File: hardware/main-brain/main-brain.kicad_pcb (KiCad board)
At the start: 2 copper layers, 140 x 70 mm, 31 parts, among them J1 19V, J2 CAN+5V, J3 19V OUT, J4 I2S OUT, Q1 SI2301 class, Q2 2N7000, U1 SN65HVD230

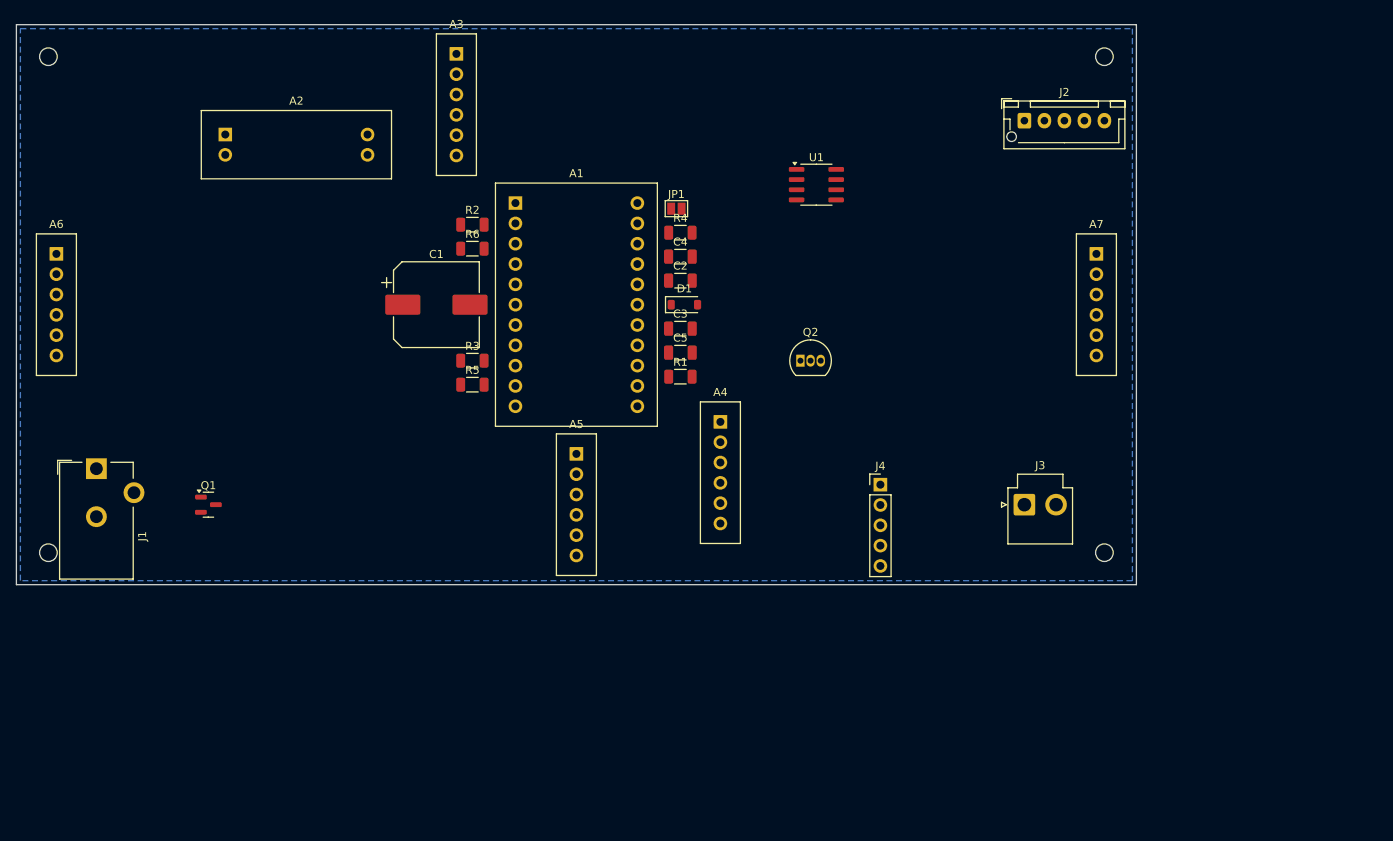
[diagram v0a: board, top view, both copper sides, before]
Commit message: Rebuild both boards from the real driver module, grouped by function
The vendor's EasyEDA export of the driver module arrived, so its footprint is
now measured rather than guessed: 17 pins and four mounting holes over
22.6 x 18.2 mm, read from vendor/simplefoc_stepmini.json at build time.

The export also settles three things that were open, and raises one:

- The module's 3V3 pin is a supply input. Its nSLEEP and nRESET pull-ups hang
  off it and there is no regulator on the board, so leaving it open would have
  left the driver possibly held in reset. It is now wired to the 3.3 V rail.
- The header's enable pin sits behind a series resistor into the driver's EN,
  so the kill line drives it directly and nSLEEP/nRESET need no connection.
- nFAULT is brought out with its own pull-up, so it now goes to PB4.
- The export shows a quad half-bridge - IN1-IN4 and OUT1-OUT4 - not the
  three-in/three-out DRV8313 the build console names. A 3-phase motor uses
  three of the four channels, so it works, but it is not the specified part.
  Flagged in the actuator README rather than silently accepted.

Placement is now by functional block. Each block keeps its own passives, and
parts with an electrical reason to hug another are placed against it and
checked: the crystal is held within 12 mm of the MCU and its load caps within
9 mm of it, which the previous layout failed at 32 mm. Microphone spacing is
pinned at exactly 130 mm and verified. Both boards are larger - the node goes
to 70 x 60 and the base to 170 x 100 - which is what buys room to group and
still route by hand.

Indicators added on both boards, using the XL-3216SURC red 1206 that is on
hand. Series resistors are sized for its 2.4 V forward drop rather than left at
a default: 220 R on 3.3 V rails, 470 R on the 5 V one.

check.py grew to match: it now verifies group membership, pinned positions and
proximity constraints alongside the netlist, and each project carries a
colour-coded placement.svg.

Co-Authored-By: Claud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
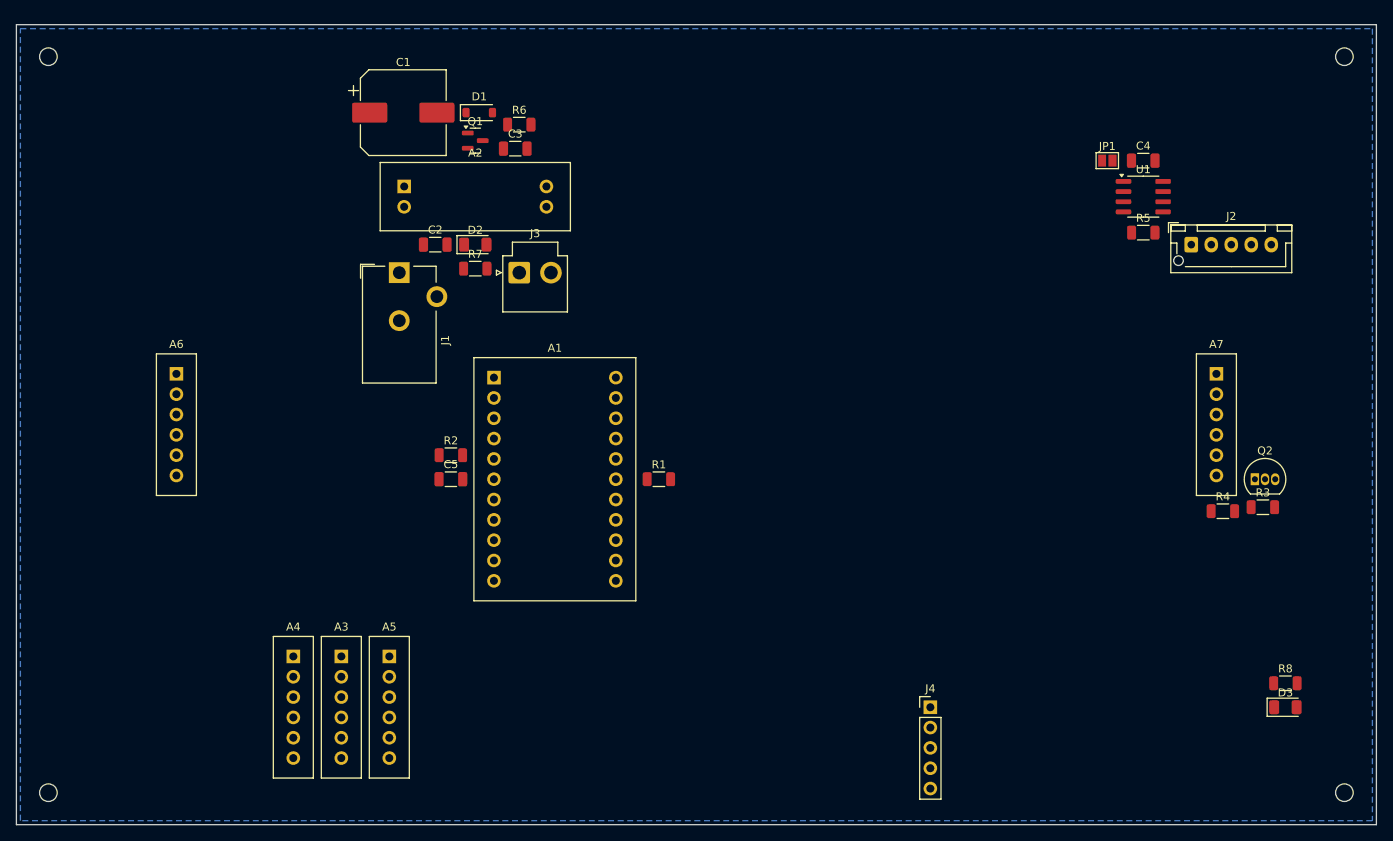
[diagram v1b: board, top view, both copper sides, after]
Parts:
- added D2: XL-3216SURC red, LED_SMD:LED_1206_3216Metric, F.Cu at (57.4, 27.5)
- added D3: XL-3216SURC red, LED_SMD:LED_1206_3216Metric, F.Cu at (158.6, 85.3)
- added R7: 470R, Resistor_SMD:R_1206_3216Metric, F.Cu at (57.4, 30.5)
- added R8: 220R, Resistor_SMD:R_1206_3216Metric, F.Cu at (158.6, 82.3)
- moved R3 100.5 mm to (155.8, 60.3)
- moved R5 86.0 mm to (140.9, 26.0)
- moved A3 76.7 mm to (40.6, 85.3)
- moved R4 76.2 mm to (150.8, 60.8)
- moved J3 69.5 mm to (62.9, 31.0)
- moved A4 60.9 mm to (34.6, 85.3)
- moved C4 59.1 mm to (140.9, 17.0)
- moved Q2 58.7 mm to (154.8, 56.8)
- moved Q1 56.4 mm to (57.4, 14.5)
- moved JP1 54.2 mm to (136.4, 17.0)
- moved J1 45.1 mm to (47.9, 31.0)
- moved ? 42.4 mm to (166.0, 96.0)
- moved U1 40.9 mm to (140.9, 21.5)
- moved D1 35.1 mm to (57.9, 11.0)
- moved A5 34.5 mm to (46.6, 85.3)
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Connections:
- A1 pad 4: (no net) -> RUN_LED_A
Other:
- board size 140 x 70 mm -> 170 x 100 mm
- board text added: "audio"
- board text added: "can"
- board text added: "i2c"
- board text added: "kill"
- board text added: "mcu"
- board text added: "power"
- board text added: "status"

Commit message: Rebuild the driver module around the real SimpleFOC Mini v1.0
The EasyEDA export the footprint was generated from was a different product:
a "step mini" quad half-bridge with IN1-IN4 and four outputs, where the board
on the bench is a SimpleFOC Mini v1.0 (DRV8313, three phases, dated 04/22).
The generated footprint carried phantom IN4/OUT4 pins, the wrong row order and
the wrong geometry, and would not have populated.

Everything now comes from the v1.0 exports. The PCB export gives pad geometry;
the schematic export resolves that PCB's anonymous U1_nn nets to real signals
and is what settled the important question below. Both step-mini exports are
removed.

Fixes a real bug this uncovered. The module's 3V3 header pin is DRV8313 pin 15,
V3P3OUT - an internal regulator output, not a supply input as previously
assumed. It had been wired to the carrier's 3.3 V rail, which would have
connected the AMS1117's output to the module's own regulator. It is now left
open, and check.py fails the build if it reappears on any net. That same
regulator feeds the module's nSlp/nRes/nFlt pull-ups, which is why those three
need no connection to idle in the running state.

The module's reference becomes A1 rather than M1, so its pins can carry the
silkscreen names M1/M2/M3 without ("M1", "M1") appearing in the netlist.

Two generator fixes fell out of the rebuild:

- simplefoc_from_json() now reads pads nested inside LIB entries, because on
  this board the headers are placed as components - only 6 of the 19 pads are
  top-level shapes - while filtering to the HDR-* components so the driver IC's
  own 29 pads stay out.
- Proximity placement follows each chain depth-first and ranks candidates by
  distance to the target's courtyard rather than to its origin. Breadth-first
  ranking by origin put a crystal load cap 3.8 mm clear of a crystal whose
  courtyard is 20 mm wide; both caps now sit inside 2 mm. check.py measures the
  same way, edge to edge, since centre-to-centre was mostly mea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
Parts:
- moved R1 27.9 mm to (54.3, 46.8)
- moved C5 13.0 mm to (54.3, 43.8)
- moved JP1 5.50 mm to (141.9, 17.0)
- moved R2 4.00 mm to (54.3, 49.8)
- moved C4 3.50 mm to (137.4, 17.0)
- moved J2 3.50 mm to (143.4, 27.5)
- moved R5 3.50 mm to (137.4, 26.0)
- moved J1 3.00 mm to (44.9, 31.0)
- moved R6 2.12 mm to (61.4, 11.0)
- moved R7 2.00 mm to (55.4, 30.5)
- moved R8 2.00 mm to (156.6, 82.3)
- moved C1 1.50 mm to (46.9, 11.0)
- moved D1 1.50 mm to (56.4, 11.0)
- moved C2 1.00 mm to (51.4, 27.5)
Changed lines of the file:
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@@
 	(footprint "Capacitor_SMD:CP_Elec_10x10.5"
 		(layer "F.Cu")
-		(at 48.36 10.996)
+		(at 46.86 10.996)
 		(descr "SMD capacitor, aluminum electrolytic, Vishay 1010, 10.0x10.5mm, http://www.vishay.com/docs/28395/150crz.pdf")
 		(tags "capacitor electrolytic")
@@
 	(footprint "Capacitor_SMD:C_1206_3216Metric"
 		(layer "F.Cu")
-		(at 52.36 27.496)
+		(at 51.36 27.496)
 		(descr "Capacitor SMD 1206 (3216 Metric), square (rectangular) end terminal, IPC_7351 nominal, (Body size source: IPC-SM-782 page 76, https://www.pcb-3d.com/wordpress/wp-content/uploads/ipc-sm-782a_amendment_1_and_2.pdf), generated with kicad-footprint-generator")
 		(tags "capacitor")
@@
 	(footprint "Capacitor_SMD:C_1206_3216Metric"
 		(layer "F.Cu")
-		(at 140.86 16.996)
+		(at 137.36 16.996)
 		(descr "Capacitor SMD 1206 (3216 Metric), square (rectangular) end terminal, IPC_7351 nominal, (Body size source: IPC-SM-782 page 76, https://www.pcb-3d.com/wordpress/wp-content/uploads/ipc-sm-782a_amendment_1_and_2.pdf), generated with kicad-footprint-generator")
 		(tags "capacitor")
@@
 	(footprint "Capacitor_SMD:C_1206_3216Metric"
 		(layer "F.Cu")
-		(at 54.31 56.818)
+		(at 54.31 43.818)
 		(descr "Capacitor SMD 1206 (3216 Metric), square (rectangular) end terminal, IPC_7351 nominal, (Body size source: IPC-SM-782 page 76, https://www.pcb-3d.com/wordpress/wp-content/uploads/ipc-sm-782a_amendment_1_and_2.pdf), generated with kicad-footprint-generator")
 		(tags "capacitor")
@@
 	(footprint "Diode_SMD:D_SOD-123"
 		(layer "F.Cu")
-		(at 57.86 10.996)
+		(at 56.36 10.996)
 		(descr "SOD-123")
 		(tags "SOD-123")
@@
 	(footprint "Connector_BarrelJack:BarrelJack_CUI_PJ-102AH_Horizontal"
 		(layer "F.Cu")
-		(at 47.86 30.996)
+		(at 44.86 30.996)
 		(descr "Thin-pin DC Barrel Jack, https://cdn-shop.adafruit.com/datasheets/21mmdcjackDatasheet.pdf")
 		(tags "Power Jack")
@@
 	(footprint "Connector_JST:JST_XH_B5B-XH-AM_1x05_P2.50mm_Vertical"
 		(layer "F.Cu")
-		(at 146.86 27.496)
+		(at 143.36 27.496)
 		(descr "JST XH series connector, B5B-XH-AM, with boss (http://www.jst-mfg.com/product/pdf/eng/eXH.pdf), generated with kicad-footprint-generator")
 		(tags "connector JST XH vertical boss")
@@
 	(footprint "Jumper:SolderJumper-2_P1.3mm_Open_Pad1.0x1.5mm"
 		(layer "F.Cu")
-		(at 136.36 16.996)
+		(at 141.86 16.996)
 		(descr "SMD Solder Jumper, 1x1.5mm Pads, 0.3mm gap, open")
 		(tags "solder jumper open")
@@
 	(footprint "Resistor_SMD:R_1206_3216Metric"
 		(layer "F.Cu")
-		(at 80.31 56.818)
+		(at 54.31 46.818)
 		(descr "Resistor SMD 1206 (3216 Metric), square (rectangular) end terminal, IPC_7351 nominal, (Body size source: IPC-SM-782 page 72, https://www.pcb-3d.com/wordpress/wp-content/uploads/ipc-sm-782a_amendment_1_and_2.pdf), generated with kicad-footprint-generator")
 		(tags "resistor")
@@
 	(footprint "Resistor_SMD:R_1206_3216Metric"
 		(layer "F.Cu")
-		(at 54.31 53.818)
+		(at 54.31 49.818)
 		(descr "Resistor SMD 1206 (3216 Metric), square (rectangular) end terminal, IPC_7351 nominal, (Body size source: IPC-SM-782 page 72, https://www.pcb-3d.com/wordpress/wp-content/uploads/ipc-sm-782a_amendment_1_and_2.pdf), generated with kicad-footprint-generator")
 		(tags "resistor")
@@
 	(footprint "Resistor_SMD:R_1206_3216Metric"
 		(layer "F.Cu")
-		(at 140.86 25.996)
+		(at 137.36 25.996)
 		(descr "Resistor SMD 1206 (3216 Metric), square (rectangular) end terminal, IPC_7351 nominal, (Body size source: IPC-SM-782 page 72, https://www.pcb-3d.com/wordpress/wp-content/uploads/ipc-sm-782a_amendment_1_and_2.pdf), generated with kicad-footprint-generator")
 		(tags "resistor")
@@
 	(footprint "Resistor_SMD:R_1206_3216Metric"
 		(layer "F.Cu")
-		(at 62.86 12.496)
+		(at 61.36 10.996)
 		(descr "Resistor SMD 1206 (3216 Metric), square (rectangular) end terminal, IPC_7351 nominal, (Body size source: IPC-SM-782 page 72, https://www.pcb-3d.com/wordpress/wp-content/uploads/ipc-sm-782a_amendment_1_and_2.pdf), generated with kicad-footprint-generator")
 		(tags "resistor")
@@
 	(footprint "Resistor_SMD:R_1206_3216Metric"
 		(layer "F.Cu")
-		(at 57.36 30.496)
+		(at 55.36 30.496)
 		(descr "Resistor SMD 1206 (3216 Metric), square (rectangular) end terminal, IPC_7351 nominal, (Body size source: IPC-SM-782 page 72, https://www.pcb-3d.com/wordpress/wp-content/uploads/ipc-sm-782a_amendment_1_and_2.pdf), generated with kicad-footprint-generator")
 		(tags "resistor")
@@
 	(footprint "Resistor_SMD:R_1206_3216Metric"
 		(layer "F.Cu")
-		(at 158.628 82.322)
+		(at 156.628 82.322)
 		(descr "Resistor SMD 1206 (3216 Metric), square (rectangular) end terminal, IPC_7351 nominal, (Body size source: IPC-SM-782 page 72, https://www.pcb-3d.com/wordpress/wp-content/uploads/ipc-sm-782a_amendment_1_and_2.pdf), generated with kicad-footprint-generator")
 		(tags "resistor")

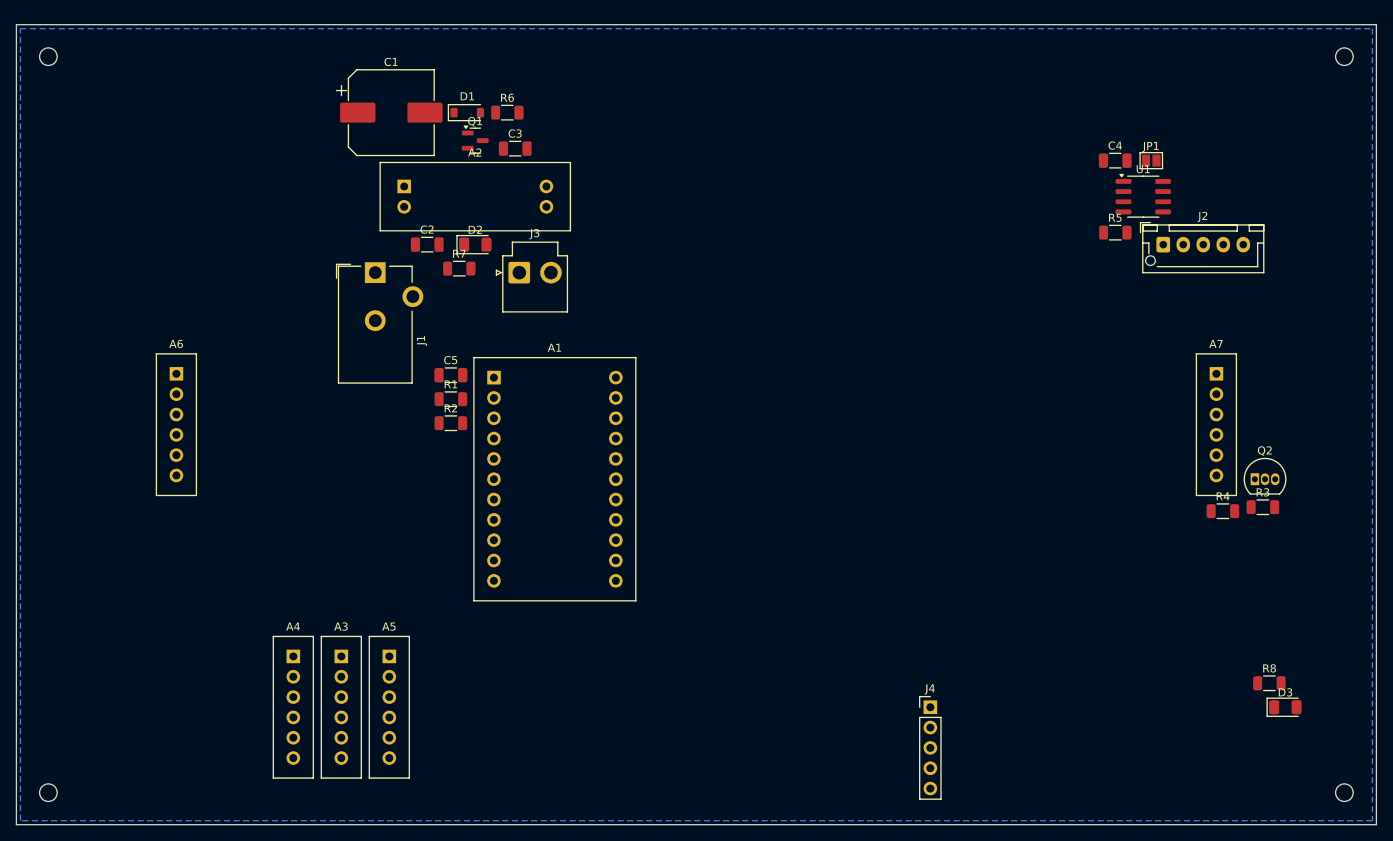
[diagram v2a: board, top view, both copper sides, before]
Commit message: Rebuild the BOM around parts on hand, and target Lion Circuits
Every passive and semiconductor in both boards is now a part that is actually
on the shelf, with docs/parts.md recording the reconciliation. Four
substitutions were needed:

- LED series resistors move from 220R/470R, which are not stocked, to 120R on
  the 3.3 V rails (7.5 mA) and 1k on the brain's 5 V rail (2.6 mA, where 120R
  would exceed the LED's 20 mA rating).
- The kill-line gate series resistor moves from 100R to 120R, immaterial here.
- The reverse-polarity FET becomes the AO3481 that is actually on hand; KiCad
  has no symbol for it, so the projects use AO3401A, the same family and the
  same G/S/D pinout.
- The 10 V zener clamping that FET's gate is not stocked, so the gate is
  divided rather than clamped: 100k source-to-gate and 100k gate-to-ground put
  Vgs at about -9.5 V, which enhances the FET hard and stays well inside its
  rating. Two resistors that are stocked, replacing one part that is not.

Two items have no substitute and must be ordered: 30 mR shunts, without which
there is no current sensing, and an N-channel MOSFET for the kill line, since
the AO3481 on hand is P-channel and cannot pull the EN bus down. The kill line
is the one circuit that should not be improvised.

Also notes that the CD43 inductor supplied with the transceivers has no place
in either board, and why the one plausible use - an LC filter on the node's
5 V input - would resonate at about 28 kHz, right on top of the motor PWM.

For fabrication, the boards now carry plot settings that emit Protel-style
gerber extensions, matching the sample set from Lion Circuits, with the X2
attributes off so the output is plain RS-274X. docs/fabrication.md records
their file naming and the design rules used, and is explicit that their
capability page could not be reached from here, so those rules are a
conservative set rather than a reading of their spec sheet.

Co-Authored-By: Claude Opus 5 <noreply@anthropic.com>
Claude-Sess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
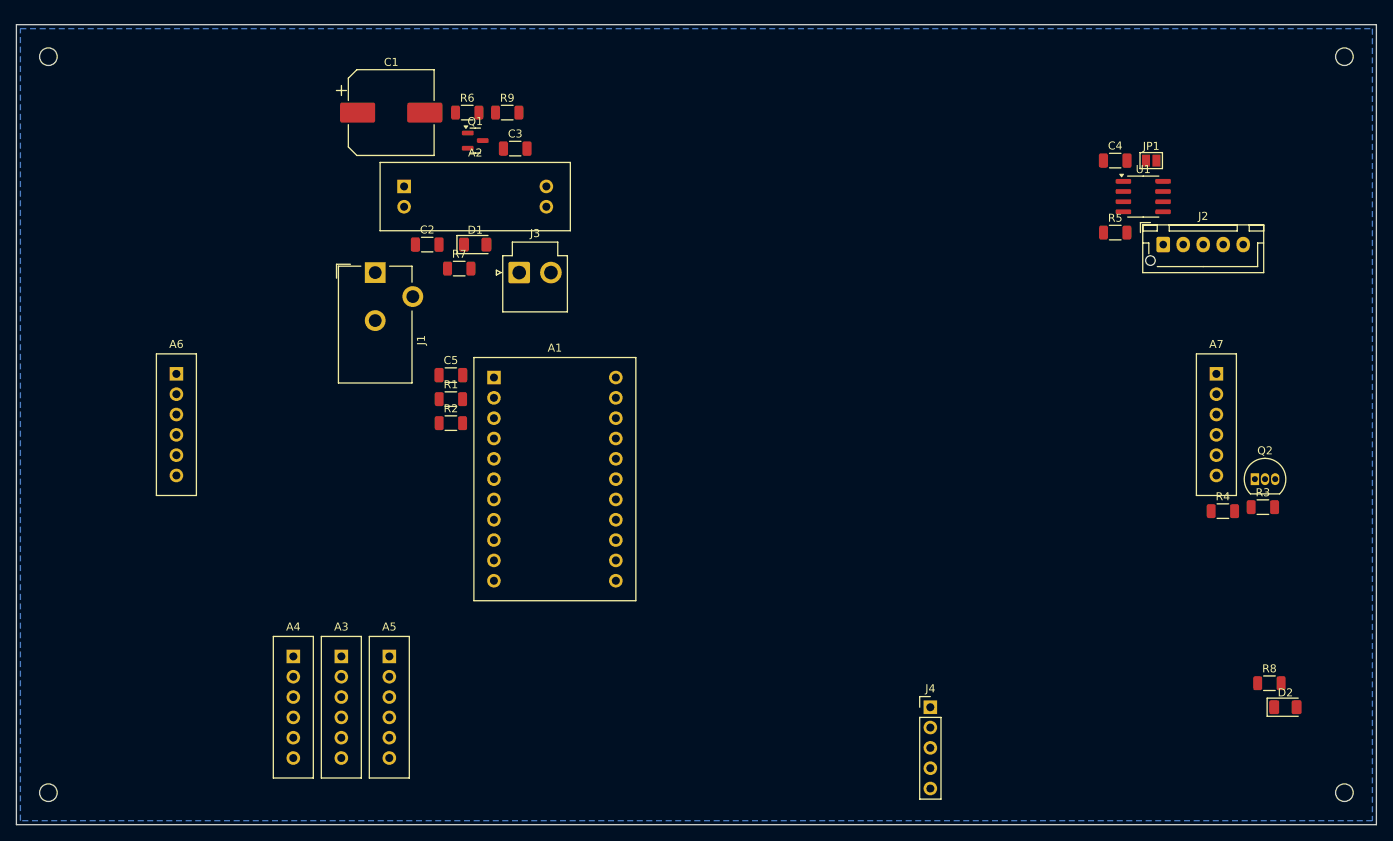
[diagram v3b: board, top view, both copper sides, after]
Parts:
- removed D3: XL-3216SURC red, LED_SMD:LED_1206_3216Metric
- added R9: 100k, Resistor_SMD:R_1206_3216Metric, F.Cu at (61.4, 11.0)
- D1: value 10V zener -> XL-3216SURC red; footprint Diode_SMD:D_SOD-123 -> LED_SMD:LED_1206_3216Metric
- Q1: value SI2301 class -> AO3481
- R4: value 100R -> 120R
- R7: value 470R -> 1k
- R8: value 220R -> 120R
- moved D2 116.6 mm to (158.6, 85.3)
- moved D1 16.5 mm to (57.4, 27.5)
- moved R6 5.01 mm to (56.4, 11.0)
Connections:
- D1 pad 1: +19V_RAW -> PWR_LED_K
- D1 pad 2: Q1_GATE -> +5V
- D2 pad 1: PWR_LED_K -> RUN_LED_K
- D2 pad 2: +5V -> RUN_LED_A
